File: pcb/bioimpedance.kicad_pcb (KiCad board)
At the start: 2 copper layers, 42.5 x 70 mm, 44 parts, among them J1 Conn_01x05_Pin, J3 USB_C_Receptacle_USB2.0_16P, J6 Conn_01x16_Pin, J8 Conn_01x16_Pin, SW5 SW_Push, SW6 SW_Push, U1 ESP32-S3-WROOM-1, U2 MAX30001CWV_T, U3 AP2112K-3.3, U4 AP2112K-1.8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

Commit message: reroute pcb
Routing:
- net BIAS: track 25.1 -> 48.7 mm, vias 1 -> 0
- net GND: track 45.2 -> 49.9 mm, vias 7 -> 9
- net INTB: track 52.2 -> 48.0 mm, vias 0 -> 2
- net +3V3: track 39.2 -> 42.6 mm, vias 6 -> 8
- net AOUT: track 40.3 -> 37.6 mm
- net Net-(U2-RBIAS): track 10.8 -> 11.8 mm, vias 0 -> 2
- net 45: track 34.0 -> 35.0 mm
- net Net-(U2-CAPN): track 3.70 -> 3.50 mm, vias 0 -> 2
- net +1V8: track 37.3 -> 37.4 mm, vias 2 -> 4
- net Net-(U2-FCLK): track 6.88 -> 7.01 mm, vias 0 -> 2

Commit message: reroute pcb AGAIN
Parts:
- moved J1 31.5 mm to (101.5, 78.7), turned to 180 degrees
- moved R2 24.3 mm to (126.1, 73.5), turned to 0 degrees
- moved R6 22.9 mm to (108.5, 79.5), turned to 0 degrees
- moved C3 22.0 mm to (110.5, 59.5), turned to 180 degrees
- moved C20 20.0 mm to (117.0, 79.5), turned to 90 degrees
- moved C19 20.0 mm to (119.0, 79.5), turned to -90 degrees
- moved C2 18.3 mm to (110.5, 61.5), turned to 180 degrees
- moved R3 18.1 mm to (108.5, 77.5), turned to 180 degrees
- moved R5 18.1 mm to (108.5, 75.5), turned to 180 degrees
- moved C21 16.7 mm to (121.9, 66.0), turned to 0 degrees
- moved C13 16.3 mm to (121.0, 75.0), turned to -90 degrees
- moved C12 15.6 mm to (121.9, 72.0), turned to 0 degrees
- moved C11 15.5 mm to (122.0, 68.0), turned to 0 degrees
- moved C10 15.0 mm to (122.0, 70.0), turned to 0 degrees
- moved R4 14.2 mm to (108.5, 73.5), turned to 180 degrees
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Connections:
- J8 pad 3: MOSI -> MISO
- J8 pad 4: MISO -> MOSI
- U1 pad 20: MISO -> MOSI
- U1 pad 21: MOSI -> MISO
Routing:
- net 14: track 50.5 -> 87.0 mm, vias 2 -> 0
- net GND: track 49.9 -> 17.2 mm, vias 9 -> 2
- net +1V8: track 37.4 -> 64.3 mm
- net CSB: track 53.1 -> 32.2 mm, vias 0 -> 2
- net INTB: track 48.0 -> 31.7 mm
- net DVRN: track 29.9 -> 45.8 mm
- net SCLK: track 59.3 -> 43.9 mm, vias 1 -> 0
- net AOUT: track 37.6 -> 22.9 mm
- net BOOT: track 56.8 -> 70.5 mm
- net 38: track 38.1 -> 27.4 mm, vias 3 -> 0
- net INT2B: track 38.7 -> 28.0 mm, vias 2 -> 0
- net RESET: track 72.5 -> 83.1 mm
- net 47: track 47.0 -> 38.0 mm, vias 2 -> 0
- net BIAS: track 48.7 -> 39.7 mm, vias 0 -> 2
- net 11: track 39.2 -> 31.0 mm, vias 2 -> 0
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
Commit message: reroute board. again
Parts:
- added C25: 10uF, Capacitor_SMD:C_0805_2012Metric, F.Cu at (104.7, 78.8)
- added C7: 0.1uF, Capacitor_SMD:C_0805_2012Metric, F.Cu at (102.7, 78.8)
- C1, C22, C4: moved to B.Cu
- moved J1 25.5 mm to (121.5, 62.9), turned to 0 degrees
- moved C21 20.2 mm to (102.2, 70.5), turned to 180 degrees
- moved R2 19.2 mm to (108.7, 65.2)
- moved R6 18.1 mm to (117.1, 63.5), turned to 180 degrees
- moved C11 16.9 mm to (105.2, 68.2), turned to 90 degrees
- moved C13 15.9 mm to (117.1, 59.5), turned to 0 degrees
- moved C10 14.9 mm to (107.2, 68.2), turned to 90 degrees
- moved R3 14.7 mm to (117.1, 65.5), turned to 0 degrees
- moved C14 13.5 mm to (117.1, 61.5), turned to 0 degrees
- moved C12 13.3 mm to (109.2, 68.2), turned to 90 degrees
- moved C9 13.3 mm to (104.7, 82.2), turned to 90 degrees
- moved R5 11.7 mm to (117.1, 67.5), turned to 0 degrees
- moved C4 10.9 mm to (109.2, 69.2), turned to 0 degrees
- moved C22 10.3 mm to (109.2, 71.2), turned to 0 degrees
- moved U2 9.83 mm to (107.0, 74.2), turned to -90 degrees
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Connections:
- J8 pad 3: MISO -> MOSI
- J8 pad 4: MOSI -> MISO
- U1 pad 20: MOSI -> MISO
- U1 pad 21: MISO -> MOSI
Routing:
- net 14: track 87.0 -> 41.5 mm, vias 0 -> 1
- net CSB: track 32.2 -> 71.5 mm, vias 2 -> 0
- net DVRN: track 45.8 -> 12.6 mm
- net AOUT: track 22.9 -> 46.5 mm
- net DVRP: track 28.1 -> 4.94 mm
- net D+: track 59.8 -> 82.2 mm
- net INT2B: track 28.0 -> 50.1 mm, vias 0 -> 2
- net D-: track 61.2 -> 80.0 mm
- net Net-(U2-FCLK): track 6.77 -> 25.1 mm
- net +1V8: track 64.3 -> 46.6 mm, vias 4 -> 2
- net Net-(U2-ECGP): track 9.98 -> 26.1 mm
- net BOOT: track 70.5 -> 55.5 mm
- net BIAS: track 39.7 -> 25.6 mm, vias 2 -> 1
- net Net-(U2-ECGN): track 9.40 -> 23.3 mm
- net SCLK: track 43.9 -> 57.5 mm
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
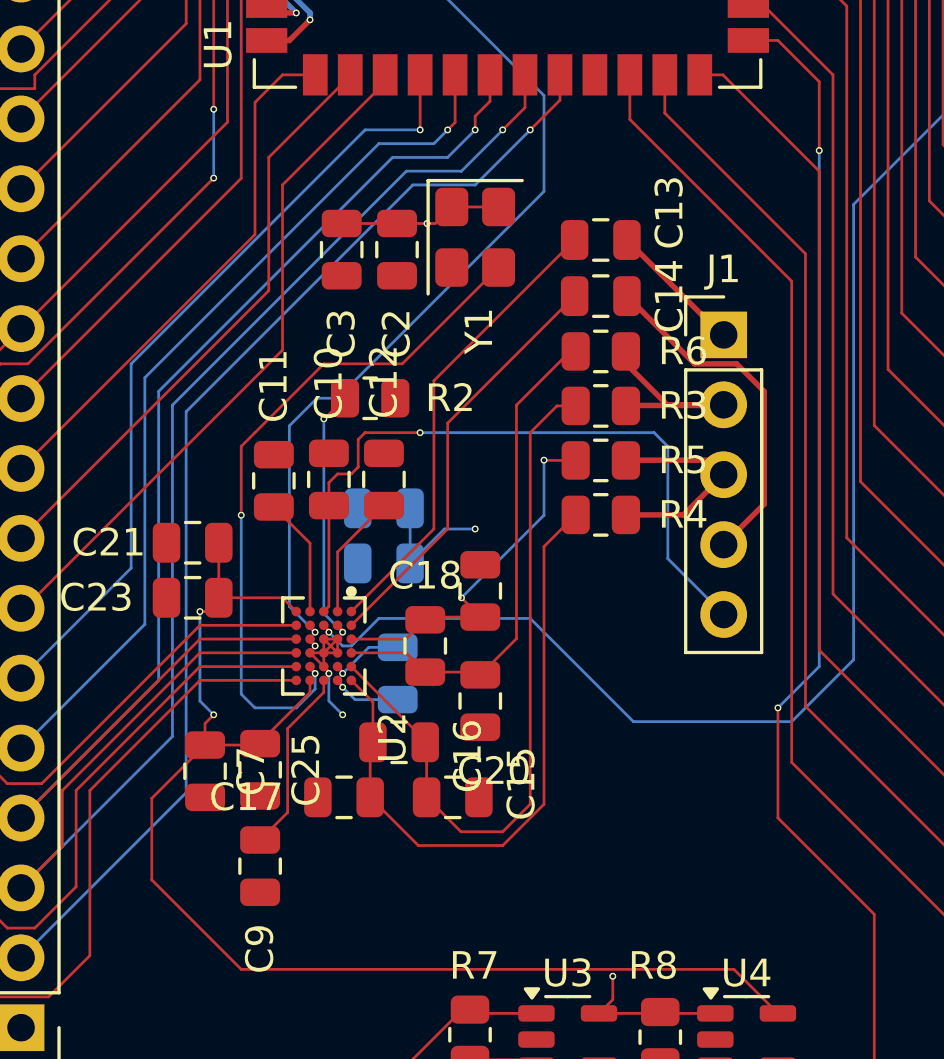
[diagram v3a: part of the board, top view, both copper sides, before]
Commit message: reroute board. again. removed copper near measurement traces
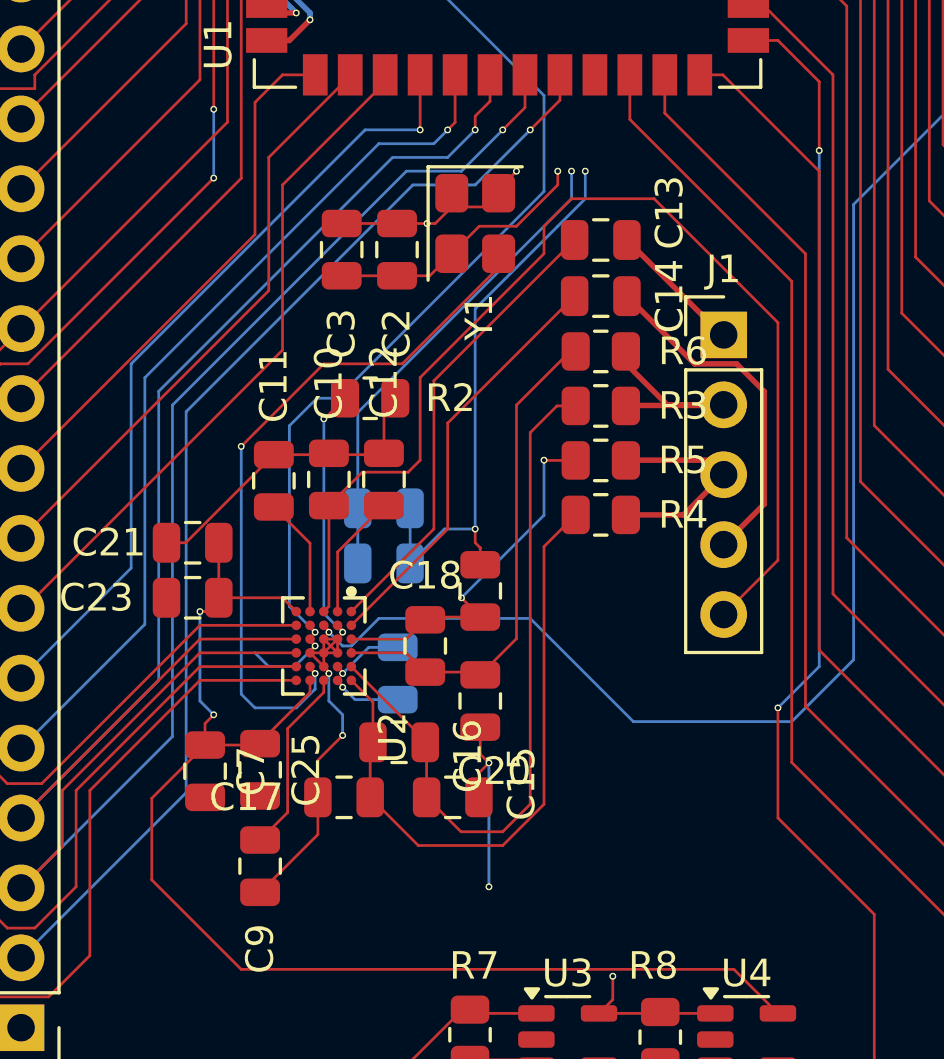
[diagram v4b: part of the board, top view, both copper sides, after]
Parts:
- moved Y1 0.50 mm to (112.5, 58.9)
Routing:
- net GND: track 12.0 -> 64.3 mm, vias 3 -> 7
- net +3V3: track 28.4 -> 50.1 mm, vias 4 -> 6
- net BIAS: track 25.6 -> 40.5 mm, vias 1 -> 0
